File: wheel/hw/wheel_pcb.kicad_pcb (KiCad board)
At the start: 2 copper layers, 36 x 67 mm, 44 parts, among them J2 DEBUG, J3 IO_C, J4 CAR, J5 IO_B, J6 IO_A, SW1 CONFIG, U1 LPC11C24FBD48, U2 TPS62175, U3 TLV70233_SOT23-5, Y1 12MHz

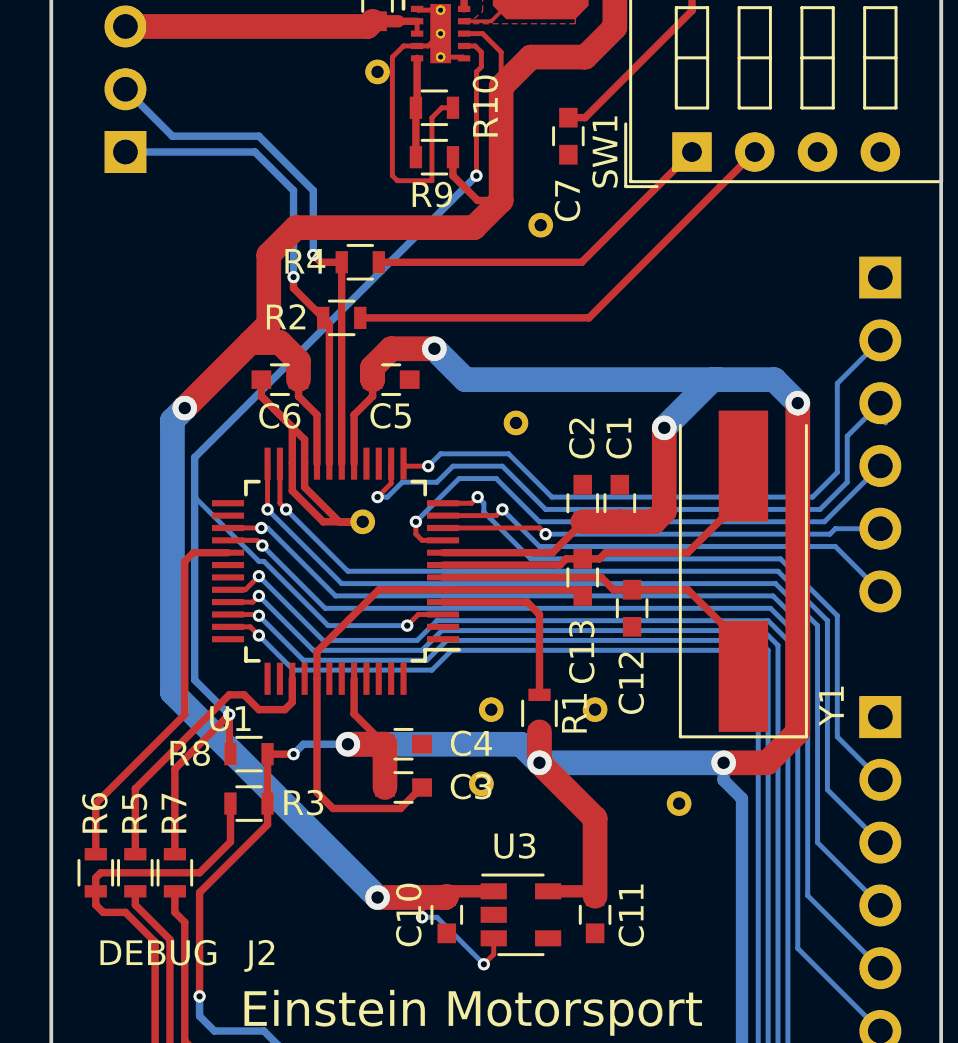
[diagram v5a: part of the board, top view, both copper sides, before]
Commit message: grounding improvements
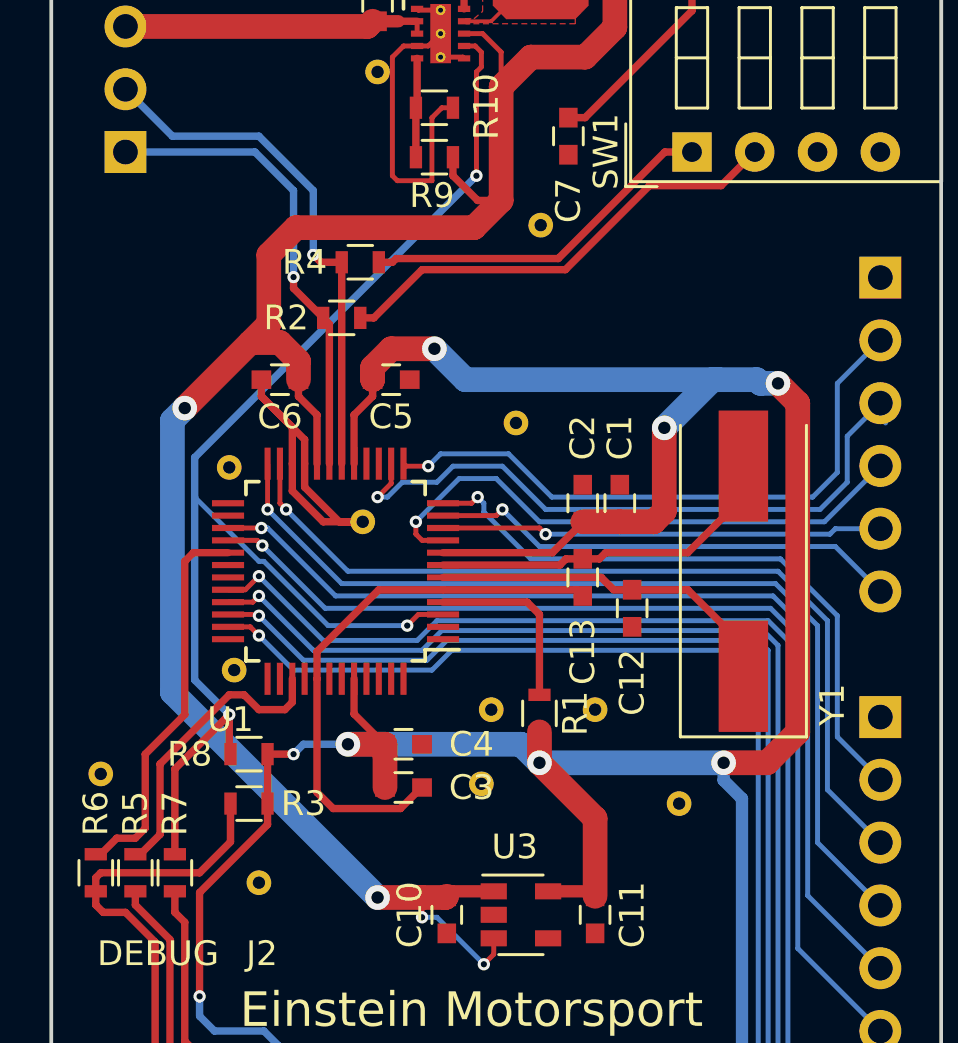
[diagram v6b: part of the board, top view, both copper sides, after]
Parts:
- added REF**: a_via, custom_footprints:a_via, B.Cu at (225.0, 91.2)
- added REF**: a_via, custom_footprints:a_via, B.Cu at (231.4, 95.6)
- added REF**: a_via, custom_footprints:a_via, B.Cu at (230.2, 78.8)
- added REF**: a_via, custom_footprints:a_via, B.Cu at (230.4, 87.0)
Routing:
- net /SWCLK: track 15.2 -> 15.8 mm
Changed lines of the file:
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@@
 (kicad_pcb (version 4) (host pcbnew 4.0.7)
   (general
-    (links 114)
+    (links 118)
     (no_connects 0)
     (area 222.375 54.924999 261.045 122.675)
     (thickness 1.6)
     (drawings 8)
-    (tracks 389)
+    (tracks 404)
     (zones 0)
-    (modules 44)
+    (modules 48)
     (nets 60)
   )
@@
   )
   (setup
-    (last_trace_width 0.5)
+    (last_trace_width 1)
     (user_trace_width 0.2)
     (user_trace_width 0.3)
@@
   )
   (module custom_footprints:a_via locked (layer B.Cu)
+    (at 225 91.2)
+    (fp_text reference REF** (at 0 -0.5) (layer B.SilkS) hide
+      (effects (font (size 1 1) (thickness 0.15)) (justify mirror))
+    )
+    (fp_text value a_via (at 0 0.5) (layer B.Fab) hide
+      (effects (font (size 1 1) (thickness 0.15)) (justify mirror))
+    )
+    (pad 1 thru_hole circle (at 0 0) (size 1 1) (drill 0.5) (layers *.Cu)
+      (net 1 GND) (zone_connect 2))
+  )
+  (module custom_footprints:a_via locked (layer B.Cu)
+    (at 231.4 95.6)
+    (fp_text reference REF** (at 0 -0.5) (layer B.SilkS) hide
+      (effects (font (size 1 1) (thickness 0.15)) (justify mirror))
+    )
+    (fp_text value a_via (at 0 0.5) (layer B.Fab) hide
+      (effects (font (size 1 1) (thickness 0.15)) (justify mirror))
+    )
+    (pad 1 thru_hole circle (at 0 0) (size 1 1) (drill 0.5) (layers *.Cu)
+      (net 1 GND) (zone_connect 2))
+  )
+  (module custom_footprints:a_via locked (layer B.Cu)
+    (at 230.2 78.8)
+    (fp_text reference REF** (at 0 -0.5) (layer B.SilkS) hide
+      (effects (font (size 1 1) (thickness 0.15)) (justify mirror))
+    )
+    (fp_text value a_via (at 0 0.5) (layer B.Fab) hide
+      (effects (font (size 1 1) (thickness 0.15)) (justify mirror))
+    )
+    (pad 1 thru_hole circle (at 0 0) (size 1 1) (drill 0.5) (layers *.Cu)
+      (net 1 GND) (zone_connect 2))
+  )
+  (module custom_footprints:a_via locked (layer B.Cu)
+    (at 230.4 87)
+    (fp_text reference REF** (at 0 -0.5) (layer B.SilkS) hide
+      (effects (font (size 1 1) (thickness 0.15)) (justify mirror))
+    )
+    (fp_text value a_via (at 0 0.5) (layer B.Fab) hide
+      (effects (font (size 1 1) (thickness 0.15)) (justify mirror))
+    )
+    (pad 1 thru_hole circle (at 0 0) (size 1 1) (drill 0.5) (layers *.Cu)
+      (net 1 GND) (zone_connect 2))
+  )
+  (module custom_footprints:a_via locked (layer B.Cu)
     (at 240.4 91.6)
     (fp_text reference REF** (at 0 -0.5) (layer B.SilkS) hide
@@
   (segment (start 239.7 60.25) (end 239.7 57.65) (width 0.3) (layer F.Cu) (net 2) (status 30))
   (segment (start 239.7 57.65) (end 239.5 57.45) (width 0.3) (layer F.Cu) (net 2) (status 30))
+  (segment (start 243.1 95.95) (end 244.8 95.95) (width 0.5) (layer F.Cu) (net 3) (status 30))
+  (segment (start 244.8 95.95) (end 245 96.15) (width 0.5) (layer F.Cu) (net 3) (status 30))
+  (segment (start 252.4 75.4) (end 253.2 76.2) (width 1) (layer F.Cu) (net 3))
+  (segment (start 253.2 76.2) (end 253.2 89.507096) (width 1) (layer F.Cu) (net 3))
+  (segment (start 251.957096 90.75) (end 250.2 90.75) (width 1) (layer F.Cu) (net 3))
+  (segment (start 253.2 89.507096) (end 251.957096 90.75) (width 1) (layer F.Cu) (net 3))
+  (segment (start 252.4 75.4) (end 251.692894 75.4) (width 1) (layer B.Cu) (net 3))
+  (segment (start 251.692894 75.4) (end 251.542894 75.25) (width 1) (layer B.Cu) (net 3))
+  (segment (start 251.542894 75.25) (end 249.75 75.25) (width 1) (layer B.Cu) (net 3))
   (segment (start 250.942894 92.2) (end 250.942894 113.782894) (width 0.5) (layer B.Cu) (net 3))
   (segment (start 250.942894 113.782894) (end 256.54 119.38) (width 0.5) (layer B.Cu) (net 3) (status 20))
   (segment (start 250.2 90.75) (end 250.2 91.457106) (width 0.5) (layer B.Cu) (net 3))
   (segment (start 250.2 91.457106) (end 250.942894 92.2) (width 0.5) (layer B.Cu) (net 3))
-  (segment (start 250.2 90.75) (end 251.957096 90.75) (width 1) (layer F.Cu) (net 3))
-  (segment (start 251.957096 90.75) (end 253.2 89.507096) (width 1) (layer F.Cu) (net 3))
-  (segment (start 253.2 89.507096) (end 253.2 76.2) (width 1) (layer F.Cu) (net 3))
   (segment (start 242.75 90.75) (end 250.2 90.75) (width 1) (layer B.Cu) (net 3))
   (via (at 250.2 90.75) (size 1) (drill 0.5) (layers F.Cu B.Cu) (net 3))
@@
   (via (at 232.8 90.4) (size 0.5) (drill 0.25) (layers F.Cu B.Cu) (net 3))
   (segment (start 235 90) (end 242 90) (width 1) (layer B.Cu) (net 3))
-  (via (at 253.2 76.2) (size 1) (drill 0.5) (layers F.Cu B.Cu) (net 3))
-  (segment (start 250 75.25) (end 252.25 75.25) (width 1) (layer B.Cu) (net 3))
-  (segment (start 252.25 75.25) (end 253.2 76.2) (width 1) (layer B.Cu) (net 3))
+  (via (at 252.4 75.4) (size 1) (drill 0.5) (layers F.Cu B.Cu) (net 3))
   (segment (start 247.8 77.2) (end 247.8 80.575) (width 1) (layer F.Cu) (net 3))
   (segment (start 247.8 80.575) (end 247.375 81) (width 1) (layer F.Cu) (net 3))
@@
   (segment (start 244.5 81.025) (end 244.5 81) (width 0.3) (layer F.Cu) (net 3) (status 30))
   (segment (start 244.5 81) (end 244.5 80.975) (width 0.5) (layer F.Cu) (net 3) (status 30))
-  (segment (start 243.1 95.95) (end 244.8 95.95) (width 0.5) (layer F.Cu) (net 3) (status 30))
-  (segment (start 244.8 95.95) (end 245 96.15) (width 0.5) (layer F.Cu) (net 3) (status 30))
   (segment (start 242 90) (end 242.75 90.75) (width 1) (layer B.Cu) (net 3))
-  (segment (start 226.4 91.8) (end 230.2 88) (width 0.3) (layer F.Cu) (net 4))
-  (segment (start 226.4 94.45) (end 226.4 91.8) (width 0.3) (layer F.Cu) (net 4) (status 10))
-  (segment (start 231.4 88.6) (end 232.45 88.6) (width 0.3) (layer F.Cu) (net 4))
-  (segment (start 232.75 87.35) (end 232.75 88.3) (width 0.3) (layer F.Cu) (net 4) (status 10))
+  (segment (start 232.75 87.35) (end 232.75 88.3) (width 0.3) (layer F.Cu) (net 4))
   (segment (start 232.75 88.3) (end 232.45 88.6) (width 0.3) (layer F.Cu) (net 4))
-  (segment (start 230.8 88) (end 231.4 88.6) (width 0.3) (layer F.Cu) (net 4))
-  (segment (start 230.2 88) (end 230.8 88) (width 0.3) (layer F.Cu) (net 4))
-  (segment (start 228.4 88.8) (end 224.8 92.4) (width 0.3) (layer F.Cu) (net 5))
-  (segment (start 224.8 94.45) (end 224.8 92.4) (width 0.3) (layer F.Cu) (net 5) (status 10))
+  (segment (start 232.45 88.6) (end 231.4 88.6) (width 0.3) (layer F.Cu) (net 4))
+  (segment (start 231.4 88.6) (end 230.8 88) (width 0.3) (layer F.Cu) (net 4))
+  (segment (start 230.8 88) (end 230.2 88) (width 0.3) (layer F.Cu) (net 4))
+  (segment (start 230.2 88) (end 227.4 90.8) (width 0.3) (layer F.Cu) (net 4))
+  (segment (start 227.4 90.8) (end 227.4 93.65) (width 0.3) (layer F.Cu) (net 4))
+  (segment (start 227.4 93.65) (end 226.6 94.45) (width 0.3) (layer F.Cu) (net 4))
+  (segment (start 226.6 94.45) (end 226.4 94.45) (width 0.3) (layer F.Cu) (net 4))
+  (segment (start 226.4 93.8) (end 225.65 93.8) (width 0.3) (layer F.Cu) (net 5))
+  (segment (start 225.65 93.8) (end 225 94.45) (width 0.3) (layer F.Cu) (net 5))
+  (segment (start 225 94.45) (end 224.8 94.45) (width 0.3) (layer F.Cu) (net 5))
+  (segment (start 226.8 93.4) (end 226.4 93.8) (width 0.3) (layer F.Cu) (net 5))
+  (segment (start 226.8 90.4) (end 226.8 93.4) (width 0.3) (layer F.Cu) (net 5))
+  (segment (start 228.4 88.8) (end 226.8 90.4) (width 0.3) (layer F.Cu) (net 5))
   (segment (start 230.15 82.25) (end 228.75 82.25) (width 0.3) (layer F.Cu) (net 5) (status 10))
   (segment (start 228.75 82.25) (end 228.4 82.6) (width 0.3) (layer F.Cu) (net 5))
@@
   (segment (start 239.7 61.75) (end 240.15 61.75) (width 0.2) (layer F.Cu) (net 37) (status 10))
   (via (at 237.4 85.2) (size 0.5) (drill 0.25) (layers F.Cu B.Cu) (net 37))
-  (segment (start 235.5 72.75) (end 244.75 72.75) (width 0.3) (layer F.Cu) (net 38) (status 10))
-  (segment (start 244.75 72.75) (end 251.46 66.04) (width 0.3) (layer F.Cu) (net 38) (status 20))
+  (segment (start 247.2 67.4) (end 250.1 67.4) (width 0.3) (layer F.Cu) (net 38))
+  (segment (start 250.1 67.4) (end 251.46 66.04) (width 0.3) (layer F.Cu) (net 38))
+  (segment (start 238 70.8) (end 243.8 70.8) (width 0.3) (layer F.Cu) (net 38))
+  (segment (start 243.8 70.8) (end 247.2 67.4) (width 0.3) (layer F.Cu) (net 38))
+  (segment (start 236.05 72.75) (end 238 70.8) (width 0.3) (layer F.Cu) (net 38))
+  (segment (start 235.5 72.75) (end 236.05 72.75) (width 0.3) (layer F.Cu) (net 38))
   (segment (start 235.5 72.75) (end 235.5 72.55) (width 0.3) (layer F.Cu) (net 38) (status 30))
-  (segment (start 236.25 70.5) (end 244.46 70.5) (width 0.3) (layer F.Cu) (net 39) (status 10))
-  (segment (start 244.46 70.5) (end 248.92 66.04) (width 0.3) (layer F.Cu) (net 39) (status 20))
+  (segment (start 247.82 66.04) (end 248.92 66.04) (width 0.3) (layer F.Cu) (net 39))
+  (segment (start 243.510009 70.349991) (end 247.82 66.04) (width 0.3) (layer F.Cu) (net 39))
+  (segment (start 236.950009 70.349991) (end 243.510009 70.349991) (width 0.3) (layer F.Cu) (net 39))
+  (segment (start 236.8 70.5) (end 236.950009 70.349991) (width 0.3) (layer F.Cu) (net 39))
+  (segment (start 236.25 70.5) (end 236.8 70.5) (width 0.3) (layer F.Cu) (net 39))
   (segment (start 236.25 70.5) (end 236.25 70.7) (width 0.3) (layer F.Cu) (net 39) (status 30))
   (segment (start 238.25 78.75) (end 238.75 78.25) (width 0.2) (layer B.Cu) (net 44))

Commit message: silkscreen
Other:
- board text added: "1:GND 2:A1 3:A2 4:A3 5:A4 6:3.3V"
- board text added: "1:GND 2:B1 3:B2 4:B3 5:B4 6:B5"
- board text added: "1:GND 2:C1 3:C2 4:C3 5:C4 6:C5"
- board text added: "Revision 1 2018-05-19"
- board text removed: "Revision 1 2018-05-18"
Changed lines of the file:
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@@
     (links 118)
     (no_connects 0)
-    (area 222.375 54.924999 261.045 122.675)
+    (area 222.924999 54.924999 259.075001 122.075001)
     (thickness 1.6)
-    (drawings 8)
+    (drawings 11)
     (tracks 404)
     (zones 0)
@@
     (tags "capacitor 0603")
     (attr smd)
-    (fp_text reference C3 (at 2.75 0) (layer F.SilkS)
+    (fp_text reference C3 (at -0.05 1.45) (layer F.SilkS)
       (effects (font (size 1 1) (thickness 0.15)))
     )
@@
     (tags "resistor 0603")
     (attr smd)
-    (fp_text reference R2 (at 2.25 0 180) (layer F.SilkS)
+    (fp_text reference R2 (at -2.45 -0.05 180) (layer F.SilkS)
       (effects (font (size 1 1) (thickness 0.15)))
     )
@@
     (tags "resistor 0603")
     (attr smd)
-    (fp_text reference R3 (at -2.2 0 180) (layer F.SilkS)
+    (fp_text reference R3 (at -2.4 0 180) (layer F.SilkS)
       (effects (font (size 1 1) (thickness 0.15)))
     )
@@
     (tags "resistor 0603")
     (attr smd)
-    (fp_text reference R4 (at 2.25 0 180) (layer F.SilkS)
+    (fp_text reference R4 (at -2.5 0 180) (layer F.SilkS)
       (effects (font (size 1 1) (thickness 0.15)))
     )
@@
     (tags "resistor 0603")
     (attr smd)
-    (fp_text reference R9 (at 0.1 -1.55 360) (layer F.SilkS)
+    (fp_text reference R9 (at 2.5 0.05 360) (layer F.SilkS)
       (effects (font (size 1 1) (thickness 0.15)))
     )
@@
     (tags "resistor 0603")
     (attr smd)
-    (fp_text reference R10 (at 2.1 -0.05 90) (layer F.SilkS)
+    (fp_text reference R10 (at -3.1 -0.05 180) (layer F.SilkS)
       (effects (font (size 1 1) (thickness 0.15)))
     )
@@
     )
   )
-  (gr_text "1:CANH\n2:CANL\n3:+12V\n4:GND" (at 235.8 62.4 180) (layer B.SilkS)
+  (gr_text "1:GND\n2:A1\n3:A2\n4:A3\n5:A4\n6:3.3V" (at 245.2 113) (layer B.SilkS)
     (effects (font (size 1.5 1.5) (thickness 0.3)) (justify left mirror))
   )
-  (gr_text "Revision 1\n2018-05-18" (at 256.8 116.4) (layer F.SilkS)
+  (gr_text "1:GND\n2:B1\n3:B2\n4:B3\n5:B4\n6:B5" (at 245.2 95.2) (layer B.SilkS)
+    (effects (font (size 1.5 1.5) (thickness 0.3)) (justify left mirror))
+  )
+  (gr_text "1:GND\n2:C1\n3:C2\n4:C3\n5:C4\n6:C5" (at 245.2 77.6) (layer B.SilkS)
+    (effects (font (size 1.5 1.5) (thickness 0.3)) (justify left mirror))
+  )
+  (gr_text "1:CANH\n2:CANL\n3:+12V\n4:GND" (at 237 62.4 180) (layer B.SilkS)
+    (effects (font (size 1.5 1.5) (thickness 0.3)) (justify left mirror))
+  )
+  (gr_text "Revision 1\n2018-05-19" (at 255 119.2) (layer F.SilkS)
     (effects (font (size 1.4 1.4) (thickness 0.28)) (justify right))
   )
-  (gr_text "Einstein Motorsport\nWheelboard\nby Thomas Watson" (at 240 103) (layer F.SilkS)
+  (gr_text "Einstein Motorsport\nWheelboard\nby Thomas Watson" (at 244 105.6) (layer F.SilkS)
     (effects (font (size 1.4 1.4) (thickness 0.28)))
   )
-  (gr_text "DIP Switch\n1: TERMINATE CANL\n2: TERMINATE CANH\n3: NOT USED\n4: NOT USED" (at 258 113) (layer B.SilkS)
-    (effects (font (size 1.4 1.4) (thickness 0.28)) (justify left mirror))
+  (gr_text "         DIP Switch\n1: TERMINATE CANL\n2: TERMINATE CANH\n3: NOT USED\n4: NOT USED" (at 223.4 115.8) (layer F.SilkS)
+    (effects (font (size 1.4 1.4) (thickness 0.28)) (justify left))
   )
   (gr_line (start 259 122) (end 259 55) (layer Edge.Cuts) (width 0.15))
